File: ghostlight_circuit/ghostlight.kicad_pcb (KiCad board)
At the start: 2 copper layers, 27 x 27 mm, 15 parts, among them IC1 STM32C011J4M6, IC2 MCP1700T-3302E_TT, IC3 LP5817DRLR, J1 Conn_01x08

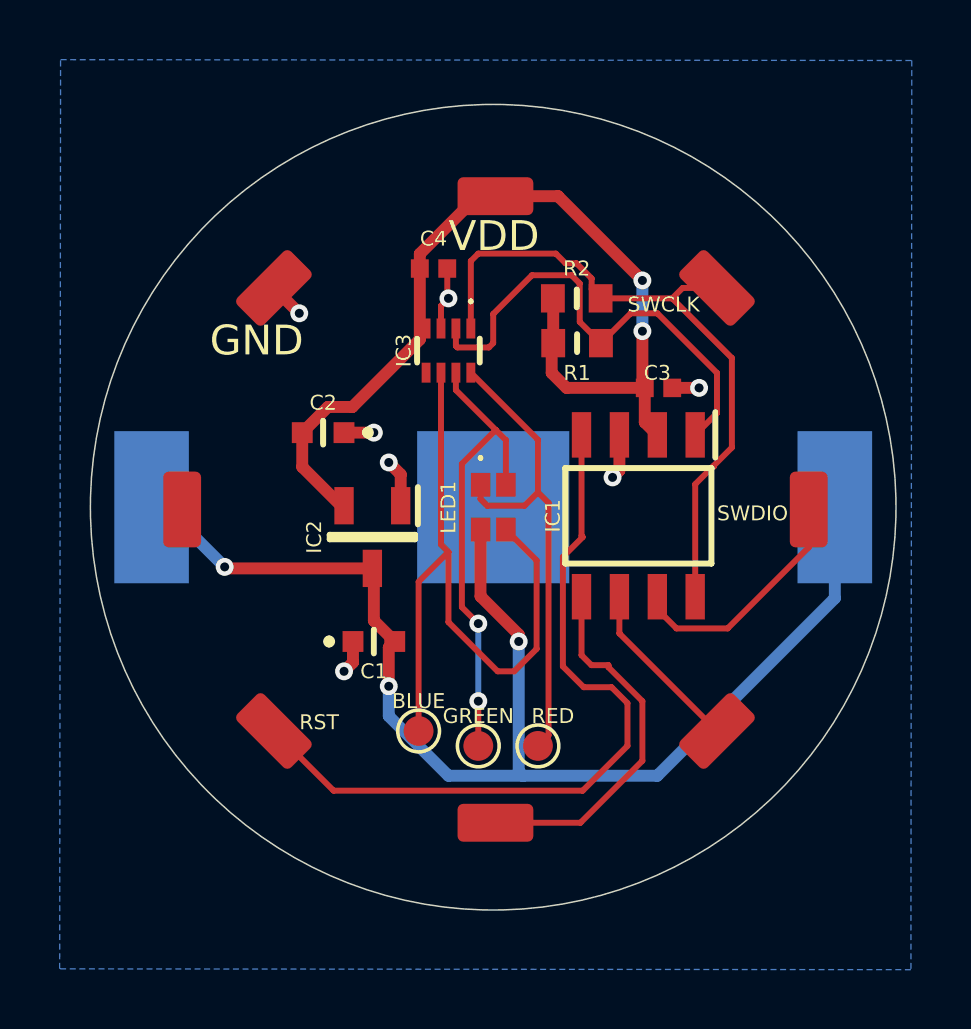
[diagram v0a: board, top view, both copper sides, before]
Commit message: update pcb
rerout and connect accelerometer

better re-route
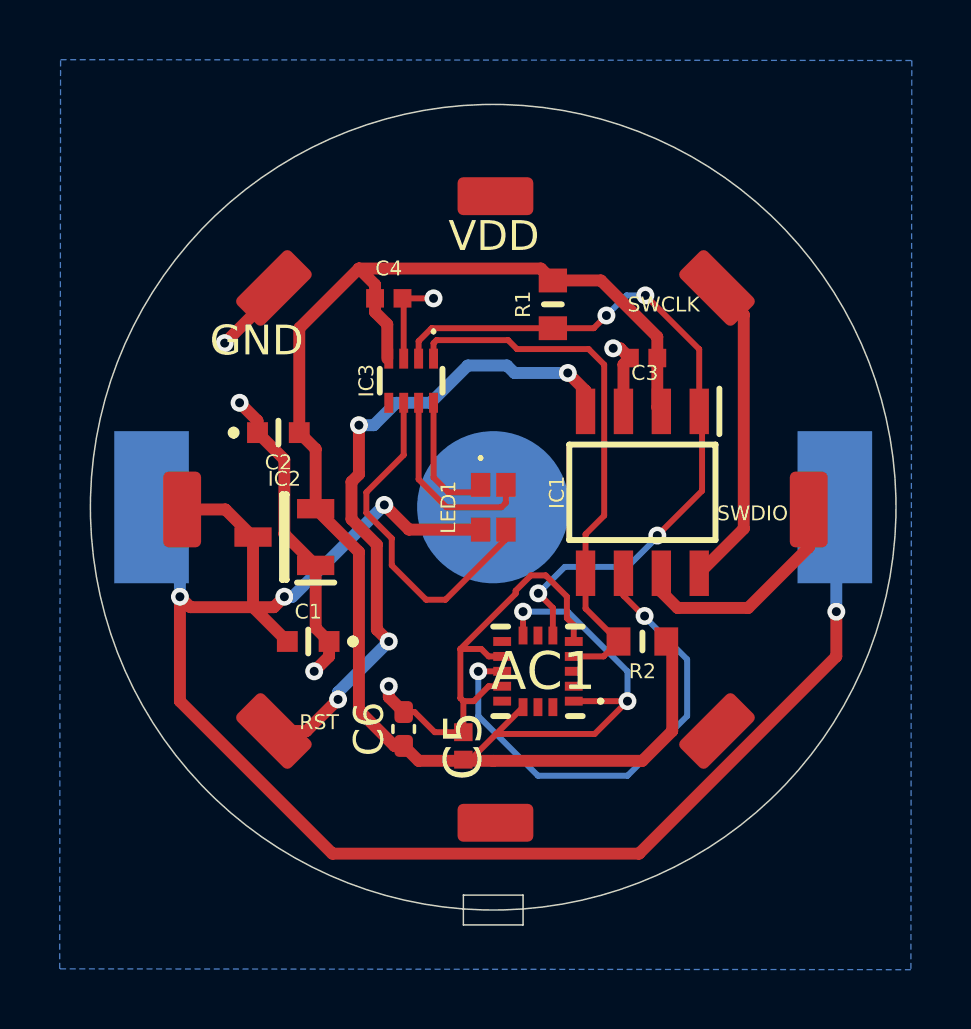
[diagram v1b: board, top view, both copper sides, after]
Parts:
- removed BLUE: TP_B, TestPoint:TestPoint_Pad_D1.0mm
- removed GREEN: TP_G, TestPoint:TestPoint_Pad_D1.0mm
- removed RED: TP_R, TestPoint:TestPoint_Pad_D1.0mm
- added AC1: LIS3DHTR, SamacSys_Parts:LIS3DHTR, F.Cu at (156.5, 105.5)
- added C5: MLASU105SB7104KFNB25, SamacSys_Parts:CAPC1005X55N, F.Cu at (154.0, 108.0)
- added C6: GRM155C80G106ME18D, Capacitor_SMD:C_0402_1005Metric_Pad0.74x0.62mm_HandSolder, F.Cu at (152.0, 107.4)
- BT1: value 3000 -> BAT-HLD-001; footprint custom_ring:Battery_Holder_Lynx_CR2032 -> custom_ring:BATHLD001mod
- moved R2 11.7 mm to (160.0, 104.5), turned to 180 degrees
- moved IC2 2.95 mm to (148.0, 101.0), turned to 180 degrees
- moved C1 2.20 mm to (148.8, 104.5), turned to 180 degrees
- moved C4 1.80 mm to (151.5, 93.0)
- moved IC3 1.61 mm to (152.2, 95.8)
- moved R1 1.53 mm to (157.0, 93.2), turned to -90 degrees
- moved C2 1.50 mm to (147.8, 97.5), turned to 0 degrees
- moved C3 1.12 mm to (160.0, 95.0), turned to 180 degrees
- moved IC1 0.80 mm to (160.0, 99.5)
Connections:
- BT1 pad 1: GND -> V_BAT
- BT1 pad 3: V_BAT -> GND
- IC1 pad 5: LIVE -> SCK
- IC1 pad 6: I2C_ERR -> ACC_INT1
- IC1 pad 8: SCK -> ST_LIKN_SWCLK
- J1 pad 2: SCK -> ST_LIKN_SWCLK
- J1 pad 4: I2C_ERR -> unconnected-(J1-Pin_4-Pad4)
- J1 pad 5: LIVE -> unconnected-(J1-Pin_5-Pad5)
- J1 pad 7: unconnected-(J1-Pin_7-Pad7) -> V_BAT
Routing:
- net 3.3V: track 32.3 -> 63.6 mm
- net GND: track 13.3 -> 34.5 mm, vias 7 -> 6
- net ACC_INT1: track 0.00 -> 16.6 mm, vias 0 -> 2
- net V_BAT: track 44.4 -> 58.3 mm, vias 3 -> 4
- net LIVE: track 12.5 -> 0.00 mm
- net Net-(IC3-OUT0): track 16.4 -> 4.39 mm
- net Net-(IC3-OUT2): track 23.3 -> 11.8 mm
- net ST_LIKN_SWCLK: track 0.00 -> 10.6 mm
- net Net-(IC3-OUT1): track 15.7 -> 6.54 mm, vias 2 -> 0
- net SDA: track 16.2 -> 24.7 mm, vias 0 -> 4
- net I2C_ERR: track 5.85 -> 0.00 mm
- net SCK: track 23.0 -> 18.3 mm
- net ST_LINK_RST/RST: track 25.5 -> 22.6 mm, vias 0 -> 4
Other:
- board size 27 x 27 mm -> 27 x 27.5 mm
